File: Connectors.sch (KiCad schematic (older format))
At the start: 4 parts

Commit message: Annotated.
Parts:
- gave numbers to parts that had none: 4
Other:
- moved on the sheet: J1, J2, J3, J4
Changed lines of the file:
@@
 $EndDescr
 $Comp
-L Connector_Generic:Conn_01x09 J?
+L Connector_Generic:Conn_01x09 J2
 U 1 1 5DA360A7
-P 5500 2325
-F 0 "J?" H 5580 2367 50  0000 L CNN
-F 1 "Conn_01x09" H 5580 2276 50  0000 L CNN
-F 2 "" H 5500 2325 50  0001 C CNN
-F 3 "~" H 5500 2325 50  0001 C CNN
-	1    5500 2325
+P 4525 4350
+F 0 "J2" H 4605 4392 50  0000 L CNN
+F 1 "Conn_01x09" H 4605 4301 50  0000 L CNN
+F 2 "" H 4525 4350 50  0001 C CNN
+F 3 "~" H 4525 4350 50  0001 C CNN
+	1    4525 4350
 	1    0    0    -1
 $EndComp
 $Comp
-L Connector_Generic:Conn_01x04 J?
+L Connector_Generic:Conn_01x04 J4
 U 1 1 5DA37217
-P 7925 3500
-F 0 "J?" H 8005 3492 50  0000 L CNN
-F 1 "Conn_01x04" H 8005 3401 50  0000 L CNN
-F 2 "" H 7925 3500 50  0001 C CNN
-F 3 "~" H 7925 3500 50  0001 C CNN
-	1    7925 3500
+P 6525 2925
+F 0 "J4" H 6605 2917 50  0000 L CNN
+F 1 "Conn_01x04" H 6605 2826 50  0000 L CNN
+F 2 "" H 6525 2925 50  0001 C CNN
+F 3 "~" H 6525 2925 50  0001 C CNN
+	1    6525 2925
 	1    0    0    -1
 $EndComp
 $Comp
-L Connector_Generic:Conn_02x03_Odd_Even J?
+L Connector_Generic:Conn_02x03_Odd_Even J3
 U 1 1 5DA37BBF
-P 5450 3725
-F 0 "J?" H 5500 4042 50  0000 C CNN
-F 1 "Conn_02x03_Odd_Even" H 5500 3951 50  0000 C CNN
-F 2 "" H 5450 3725 50  0001 C CNN
-F 3 "~" H 5450 3725 50  0001 C CNN
-	1    5450 3725
+P 6500 4475
+F 0 "J3" H 6550 4792 50  0000 C CNN
+F 1 "Conn_02x03_Odd_Even" H 6550 4701 50  0000 C CNN
+F 2 "" H 6500 4475 50  0001 C CNN
+F 3 "~" H 6500 4475 50  0001 C CNN
+	1    6500 4475
 	1    0    0    -1
 $EndComp
 $Comp
-L Connector_Generic:Conn_01x04 J?
+L Connector_Generic:Conn_01x04 J1
 U 1 1 5DA389EB
-P 7925 2275
-F 0 "J?" H 8005 2267 50  0000 L CNN
-F 1 "Conn_01x04" H 8005 2176 50  0000 L CNN
-F 2 "" H 7925 2275 50  0001 C CNN
-F 3 "~" H 7925 2275 50  0001 C CNN
-	1    7925 2275
+P 4500 2925
+F 0 "J1" H 4580 2917 50  0000 L CNN
+F 1 "Conn_01x04" H 4580 2826 50  0000 L CNN
+F 2 "" H 4500 2925 50  0001 C CNN
+F 3 "~" H 4500 2925 50  0001 C CNN
+	1    4500 2925
 	1    0    0    -1
 $EndComp

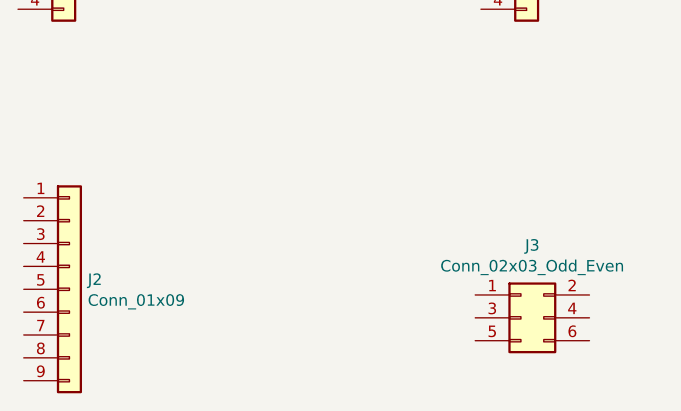
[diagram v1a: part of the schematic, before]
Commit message: Footprints assigned.
Review with real footprints that I'm going to use.
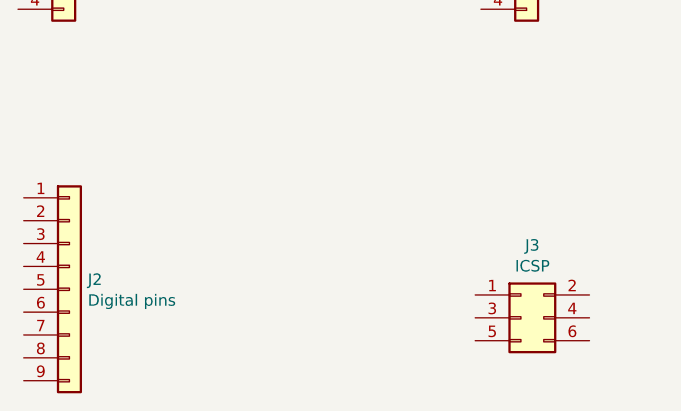
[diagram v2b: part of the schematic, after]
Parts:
- J1, J4: footprint (none) -> Connector_PinSocket_2.54mm:PinSocket_1x04_P2.54mm_Vertical
- J2: value Conn_01x09 -> Digital pins; footprint (none) -> Connector_PinSocket_2.54mm:PinSocket_1x09_P2.54mm_Vertical
- J3: value Conn_02x03_Odd_Even -> ICSP; footprint (none) -> Connector_PinSocket_2.54mm:PinSocket_2x03_P2.54mm_Vertical
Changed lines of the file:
@@
 P 4525 4350
 F 0 "J2" H 4605 4392 50  0000 L CNN
-F 1 "Conn_01x09" H 4605 4301 50  0000 L CNN
-F 2 "" H 4525 4350 50  0001 C CNN
+F 1 "Digital pins" H 4605 4301 50  0000 L CNN
+F 2 "Connector_PinSocket_2.54mm:PinSocket_1x09_P2.54mm_Vertical" H 4525 4350 50  0001 C CNN
 F 3 "~" H 4525 4350 50  0001 C CNN
 	1    4525 4350
@@
 F 0 "J4" H 6605 2917 50  0000 L CNN
 F 1 "Conn_01x04" H 6605 2826 50  0000 L CNN
-F 2 "" H 6525 2925 50  0001 C CNN
+F 2 "Connector_PinSocket_2.54mm:PinSocket_1x04_P2.54mm_Vertical" H 6525 2925 50  0001 C CNN
 F 3 "~" H 6525 2925 50  0001 C CNN
 	1    6525 2925
@@
 P 6500 4475
 F 0 "J3" H 6550 4792 50  0000 C CNN
-F 1 "Conn_02x03_Odd_Even" H 6550 4701 50  0000 C CNN
-F 2 "" H 6500 4475 50  0001 C CNN
+F 1 "ICSP" H 6550 4701 50  0000 C CNN
+F 2 "Connector_PinSocket_2.54mm:PinSocket_2x03_P2.54mm_Vertical" H 6500 4475 50  0001 C CNN
 F 3 "~" H 6500 4475 50  0001 C CNN
 	1    6500 4475
@@
 F 0 "J1" H 4580 2917 50  0000 L CNN
 F 1 "Conn_01x04" H 4580 2826 50  0000 L CNN
-F 2 "" H 4500 2925 50  0001 C CNN
+F 2 "Connector_PinSocket_2.54mm:PinSocket_1x04_P2.54mm_Vertical" H 4500 2925 50  0001 C CNN
 F 3 "~" H 4500 2925 50  0001 C CNN
 	1    4500 2925

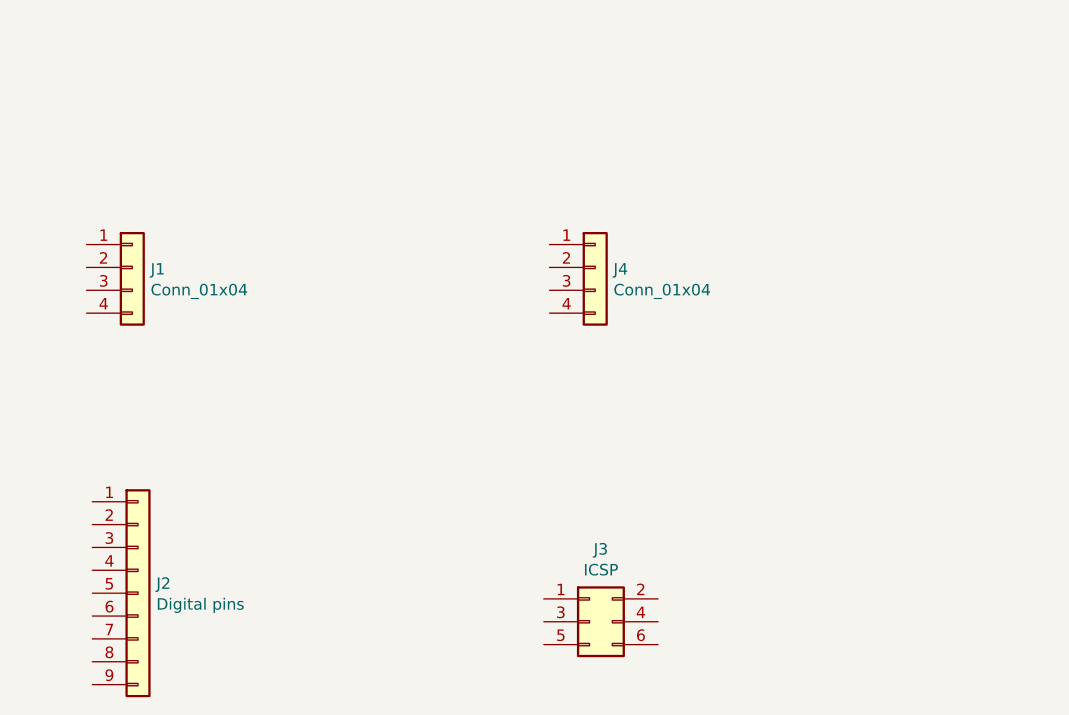
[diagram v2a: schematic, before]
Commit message: Place labels on connectors sheet & wire
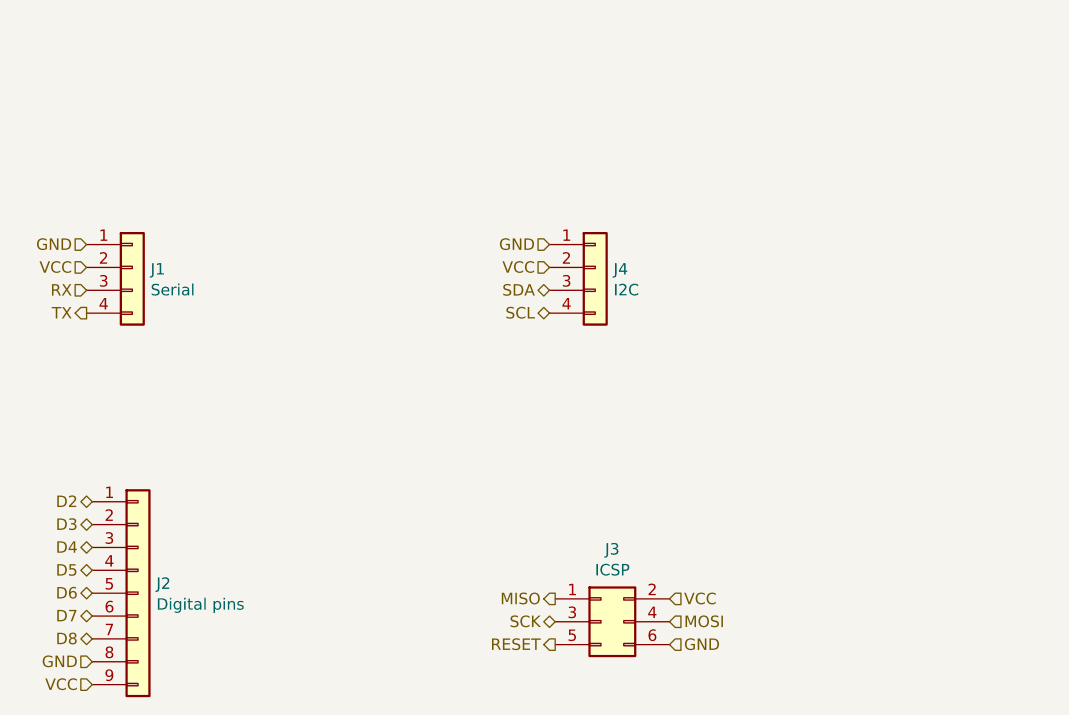
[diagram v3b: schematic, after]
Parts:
- J1: value Conn_01x04 -> Serial
- J4: value Conn_01x04 -> I2C
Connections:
- net D2: now reaches J2.1 (Pin_1)
- net D3: now reaches J2.2 (Pin_2)
- net D4: now reaches J2.3 (Pin_3)
- net D5: now reaches J2.4 (Pin_4)
- net D6: now reaches J2.5 (Pin_5)
- net D7: now reaches J2.6 (Pin_6)
- net D8: now reaches J2.7 (Pin_7)
- net GND: now reaches J2.8 (Pin_8)
- net GND: now also J1.1 (Pin_1), J3.6 (Pin_6), J4.1 (Pin_1)
- net VCC: now reaches J2.9 (Pin_9)
- net VCC: now also J1.2 (Pin_2), J3.2 (Pin_2), J4.2 (Pin_2)
- net SDA: now reaches J4.3 (Pin_3)
- net SCL: now reaches J4.4 (Pin_4)
- net MISO: now reaches J3.1 (Pin_1)
- net SCK: now reaches J3.3 (Pin_3)
- net MOSI: now reaches J3.4 (Pin_4)
- net RESET: now reaches J3.5 (Pin_5)
- net RX: now reaches J1.3 (Pin_3)
- net TX: now reaches J1.4 (Pin_4)
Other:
- moved on the sheet: J3
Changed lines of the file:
@@
 P 6525 2925
 F 0 "J4" H 6605 2917 50  0000 L CNN
-F 1 "Conn_01x04" H 6605 2826 50  0000 L CNN
+F 1 "I2C" H 6605 2826 50  0000 L CNN
 F 2 "Connector_PinSocket_2.54mm:PinSocket_1x04_P2.54mm_Vertical" H 6525 2925 50  0001 C CNN
 F 3 "~" H 6525 2925 50  0001 C CNN
@@
 L Connector_Generic:Conn_02x03_Odd_Even J3
 U 1 1 5DA37BBF
-P 6500 4475
-F 0 "J3" H 6550 4792 50  0000 C CNN
-F 1 "ICSP" H 6550 4701 50  0000 C CNN
-F 2 "Connector_PinSocket_2.54mm:PinSocket_2x03_P2.54mm_Vertical" H 6500 4475 50  0001 C CNN
-F 3 "~" H 6500 4475 50  0001 C CNN
-	1    6500 4475
+P 6550 4475
+F 0 "J3" H 6600 4792 50  0000 C CNN
+F 1 "ICSP" H 6600 4701 50  0000 C CNN
+F 2 "Connector_PinSocket_2.54mm:PinSocket_2x03_P2.54mm_Vertical" H 6550 4475 50  0001 C CNN
+F 3 "~" H 6550 4475 50  0001 C CNN
+	1    6550 4475
 	1    0    0    -1
 $EndComp
@@
 P 4500 2925
 F 0 "J1" H 4580 2917 50  0000 L CNN
-F 1 "Conn_01x04" H 4580 2826 50  0000 L CNN
+F 1 "Serial" H 4580 2826 50  0000 L CNN
 F 2 "Connector_PinSocket_2.54mm:PinSocket_1x04_P2.54mm_Vertical" H 4500 2925 50  0001 C CNN
 F 3 "~" H 4500 2925 50  0001 C CNN
@@
 	1    0    0    -1
 $EndComp
+Text HLabel 6350 4375 0    50   Output ~ 0
+MISO
+Text HLabel 6350 4475 0    50   BiDi ~ 0
+SCK
+Text HLabel 6850 4375 2    50   Input ~ 0
+VCC
+Text HLabel 6350 4575 0    50   Output ~ 0
+RESET
+Text HLabel 6850 4475 2    50   Input ~ 0
+MOSI
+Text HLabel 6850 4575 2    50   Input ~ 0
+GND
+Text HLabel 4300 2825 0    50   Input ~ 0
+GND
+Text HLabel 4300 2925 0    50   Input ~ 0
+VCC
+Text HLabel 4300 3025 0    50   Input ~ 0
+RX
+Text HLabel 4300 3125 0    50   Output ~ 0
+TX
+Text HLabel 6325 2825 0    50   Input ~ 0
+GND
+Text HLabel 6325 2925 0    50   Input ~ 0
+VCC
+Text HLabel 6325 3025 0    50   BiDi ~ 0
+SDA
+Text HLabel 6325 3125 0    50   BiDi ~ 0
+SCL
+Text HLabel 4325 3950 0    50   BiDi ~ 0
+D2
+Text HLabel 4325 4050 0    50   BiDi ~ 0
+D3
+Text HLabel 4325 4150 0    50   BiDi ~ 0
+D4
+Text HLabel 4325 4250 0    50   BiDi ~ 0
+D5
+Text HLabel 4325 4350 0    50   BiDi ~ 0
+D6
+Text HLabel 4325 4450 0    50   BiDi ~ 0
+D7
+Text HLabel 4325 4550 0    50   BiDi ~ 0
+D8
+Text HLabel 4325 4650 0    50   Input ~ 0
+GND
+Text HLabel 4325 4750 0    50   Input ~ 0
+VCC
 $EndSCHEMATC

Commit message: Comment sections and generate netlist
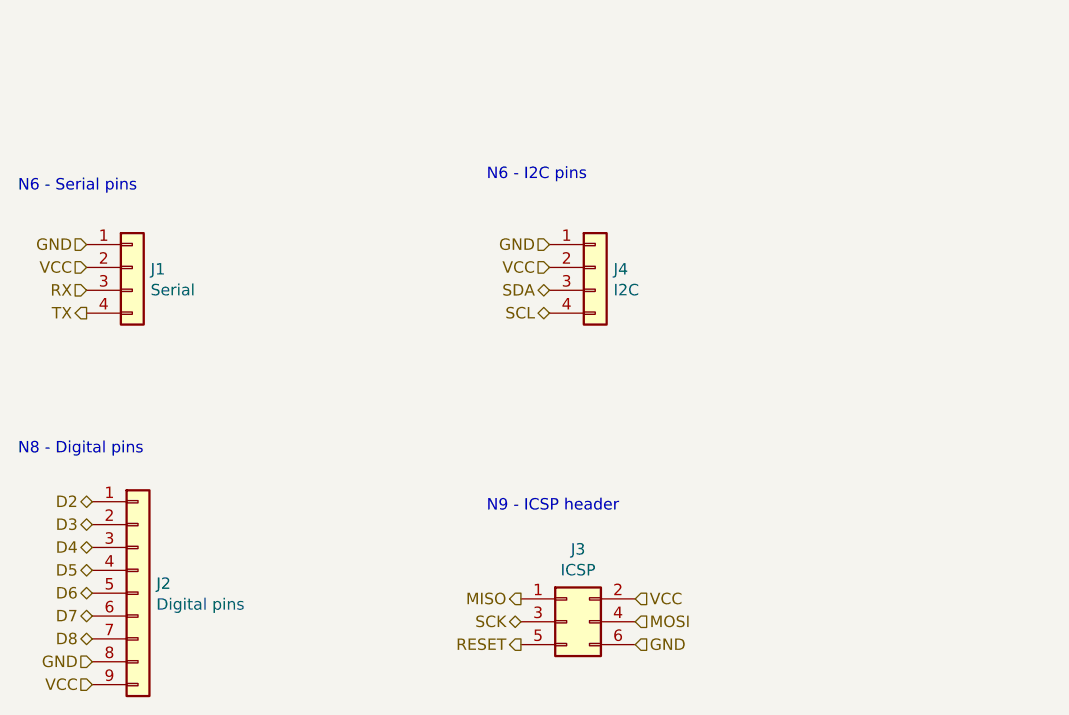
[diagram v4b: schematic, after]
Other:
- note added: "N6 - I2C pins"
- note added: "N6 - Serial pins"
- note added: "N8 - Digital pins"
- note added: "N9 - ICSP header"
- moved on the sheet: J3
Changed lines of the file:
@@
 L Connector_Generic:Conn_02x03_Odd_Even J3
 U 1 1 5DA37BBF
-P 6550 4475
-F 0 "J3" H 6600 4792 50  0000 C CNN
-F 1 "ICSP" H 6600 4701 50  0000 C CNN
-F 2 "Connector_PinSocket_2.54mm:PinSocket_2x03_P2.54mm_Vertical" H 6550 4475 50  0001 C CNN
-F 3 "~" H 6550 4475 50  0001 C CNN
-	1    6550 4475
+P 6400 4475
+F 0 "J3" H 6450 4792 50  0000 C CNN
+F 1 "ICSP" H 6450 4701 50  0000 C CNN
+F 2 "Connector_PinSocket_2.54mm:PinSocket_2x03_P2.54mm_Vertical" H 6400 4475 50  0001 C CNN
+F 3 "~" H 6400 4475 50  0001 C CNN
+	1    6400 4475
 	1    0    0    -1
 $EndComp
@@
 	1    0    0    -1
 $EndComp
-Text HLabel 6350 4375 0    50   Output ~ 0
+Text HLabel 6200 4375 0    50   Output ~ 0
 MISO
-Text HLabel 6350 4475 0    50   BiDi ~ 0
+Text HLabel 6200 4475 0    50   BiDi ~ 0
 SCK
-Text HLabel 6850 4375 2    50   Input ~ 0
+Text HLabel 6700 4375 2    50   Input ~ 0
 VCC
-Text HLabel 6350 4575 0    50   Output ~ 0
+Text HLabel 6200 4575 0    50   Output ~ 0
 RESET
-Text HLabel 6850 4475 2    50   Input ~ 0
+Text HLabel 6700 4475 2    50   Input ~ 0
 MOSI
-Text HLabel 6850 4575 2    50   Input ~ 0
+Text HLabel 6700 4575 2    50   Input ~ 0
 GND
 Text HLabel 4300 2825 0    50   Input ~ 0
@@
 Text HLabel 4325 4750 0    50   Input ~ 0
 VCC
+Text Notes 4000 2600 0    50   ~ 0
+N6 - Serial pins
+Text Notes 6050 2550 0    50   ~ 0
+N6 - I2C pins
+Text Notes 4000 3750 0    50   ~ 0
+N8 - Digital pins
+Text Notes 6050 4000 0    50   ~ 0
+N9 - ICSP header
 $EndSCHEMATC
